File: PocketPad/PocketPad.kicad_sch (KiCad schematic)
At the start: 41 parts, among them SW0 SW_Push, SW1 SW_Push, SW10 SW_Push, SW11 SW_Push, SW12 SW_Push, SW13 SW_Push, SW14 SW_Push, SW15 SW_Push, SW16 SW_Push, SW17 SW_Push, SW18 SW_Push, SW2 SW_Push, SW3 SW_Push, SW4 SW_Push, SW5 SW_Push, SW6 SW_Push, SW7 SW_Push, SW8 SW_Push, SW9 SW_Push

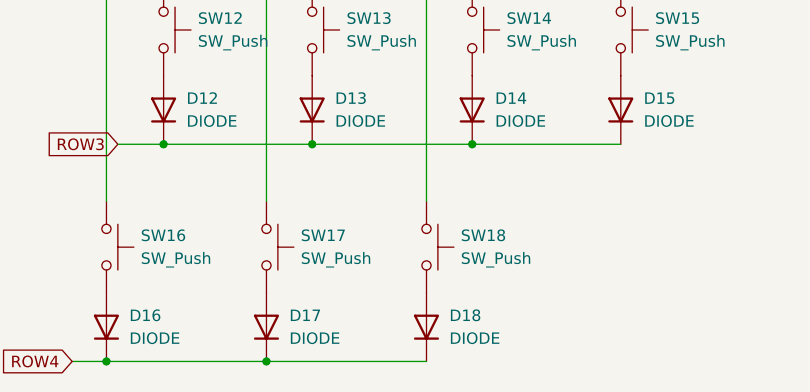
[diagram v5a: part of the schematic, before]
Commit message: V0.2 : Removed SW18
Redid trace routes. Removed SW18, moved SW16,17 over. Moved PWR & ACT LEDs
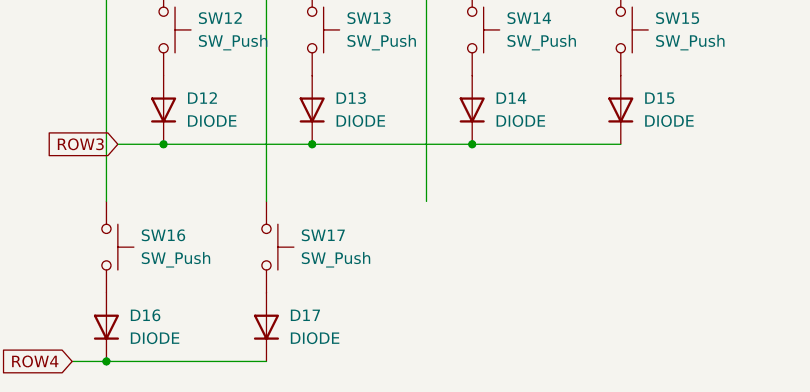
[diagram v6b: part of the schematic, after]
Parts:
- removed D18: DIODE, Diode_THT:D_DO-35_SOD27_P7.62mm_Horizontal, symbol Simulation_SPICE:DIODE
- removed SW18: SW_Push, Keebio:Switch_THT_6x6x8.5, symbol Switch:SW_Push
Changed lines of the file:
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@@
   (junction (at 102.87 67.31) (diameter 0) (color 0 0 0 0)
   )
-  (junction (at 91.44 129.54) (diameter 0) (color 0 0 0 0)
-  )
   (junction (at 100.33 43.18) (diameter 0) (color 0 0 0 0)
   )
@@
   )
   (wire (pts (xy 96.52 105.41) (xy 114.3 105.41))
-    (stroke (width 0) (type default) (color 0 0 0 0))
-  )
-  (wire (pts (xy 91.44 129.54) (xy 109.22 129.54))
     (stroke (width 0) (type default) (color 0 0 0 0))
   )
@@
     (pin "2")
   )
-  (symbol (lib_id "Switch:SW_Push") (at 109.22 116.84 270) (unit 1)
-    (in_bom yes) (on_board yes) (fields_autoplaced)
-    (property "Reference" "SW18" (id 0) (at 113.03 115.5699 90)
-      (effects (font (size 1.27 1.27)) (justify left))
-    )
-    (property "Value" "SW_Push" (id 1) (at 113.03 118.1099 90)
-      (effects (font (size 1.27 1.27)) (justify left))
-    )
-    (property "Footprint" "Keebio:Switch_THT_6x6x8.5" (id 2) (at 114.3 116.84 0)
-      (effects (font (size 1.27 1.27)) hide)
-    )
-    (property "Datasheet" "~" (id 3) (at 114.3 116.84 0)
-      (effects (font (size 1.27 1.27)) hide)
-    )
-    (pin "1")
-    (pin "2")
-  )
   (symbol (lib_id "Simulation_SPICE:DIODE") (at 116.84 39.37 270) (unit 1)
     (in_bom yes) (on_board yes) (fields_autoplaced)
@@
     (property "Datasheet" "~" (id 3) (at 133.35 50.8 0)
       (effects (font (size 1.27 1.27)) hide)
-    )
-    (pin "1")
-    (pin "2")
-  )
-  (symbol (lib_id "Simulation_SPICE:DIODE") (at 109.22 125.73 270) (unit 1)
-    (in_bom yes) (on_board yes) (fields_autoplaced)
-    (property "Reference" "D18" (id 0) (at 111.76 124.4599 90)
-      (effects (font (size 1.27 1.27)) (justify left))
-    )
-    (property "Value" "DIODE" (id 1) (at 111.76 126.9999 90)
-      (effects (font (size 1.27 1.27)) (justify left))
-    )
-    (property "Footprint" "Diode_THT:D_DO-35_SOD27_P7.62mm_Horizontal" (id 2) (at 109.22 125.73 0)
-      (effects (font (size 1.27 1.27)) hide)
-    )
-    (property "Datasheet" "~" (id 3) (at 109.22 125.73 0)
-      (effects (font (size 1.27 1.27)) hide)
-    )
-    (property "Spice_Netlist_Enabled" "Y" (id 4) (at 109.22 125.73 0)
-      (effects (font (size 1.27 1.27)) (justify left) hide)
-    )
-    (property "Spice_Primitive" "D" (id 5) (at 109.22 125.73 0)
-      (effects (font (size 1.27 1.27)) (justify left) hide)
     )
     (pin "1")
@@
       (reference "D17") (unit 1) (value "DIODE") (footprint "Diode_THT:D_DO-35_SOD27_P7.62mm_Horizontal")
     )
-    (path "/4d9a6203-d8f3-47c1-9521-23a9923c6132"
-      (reference "D18") (unit 1) (value "DIODE") (footprint "Diode_THT:D_DO-35_SOD27_P7.62mm_Horizontal")
-    )
     (path "/997ac6b3-feea-4945-b5ae-fc1302bd8731"
       (reference "MCU1") (unit 1) (value "Elite-C") (footprint "Keebio:Elite-C")
@@
       (reference "SW17") (unit 1) (value "SW_Push") (footprint "Keebio:Switch_THT_6x6x8.5")
     )
-    (path "/3ee2405a-2fc8-460e-9619-5b5c330637fc"
-      (reference "SW18") (unit 1) (value "SW_Push") (footprint "Keebio:Switch_THT_6x6x8.5")
-    )
-  )
+  )

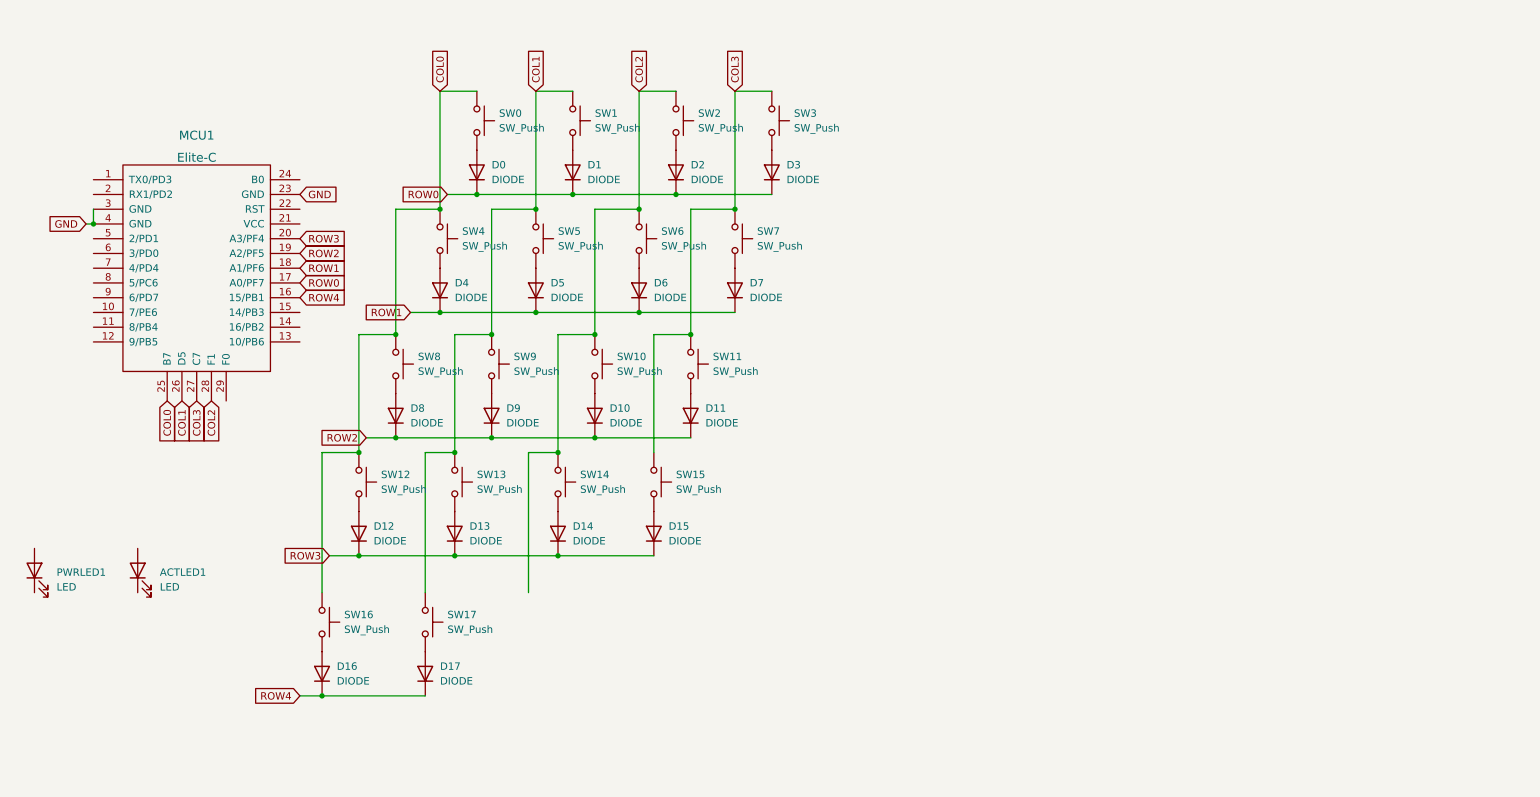
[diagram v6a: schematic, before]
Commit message: symbols updated. PCB redone.
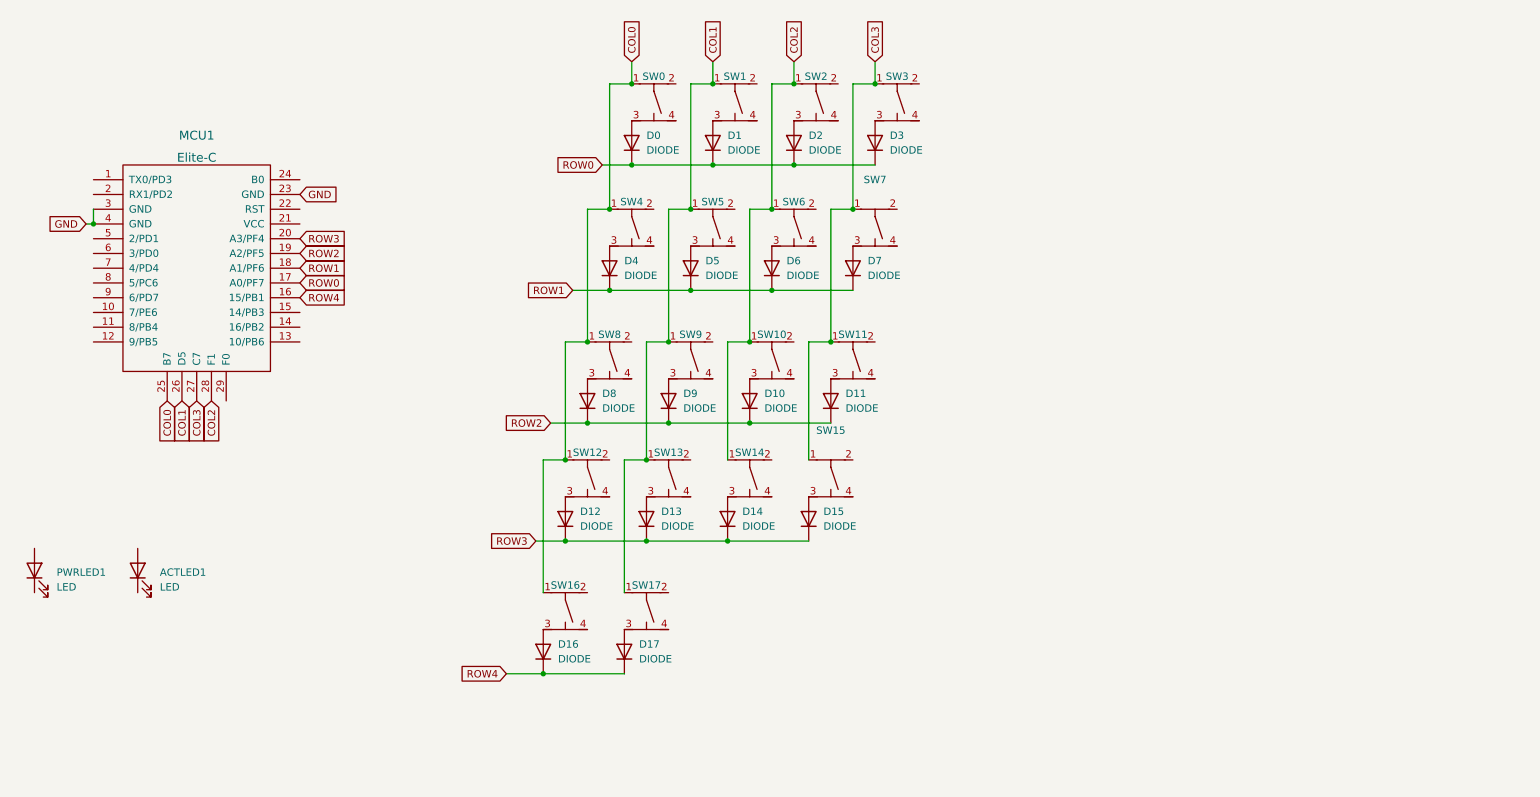
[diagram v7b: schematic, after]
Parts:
- removed SW0, SW1, SW10, SW11, SW12, SW13, SW14, SW15, SW16, SW17, SW2, SW3, SW4, SW5, SW6, SW7, SW8, SW9: SW_Push, Keebio:Switch_THT_6x6x8.5, symbol Switch:SW_Push
- added SW0, SW1, SW10, SW11, SW12, SW13, SW14, SW15, SW16, SW17, SW2, SW3, SW4, SW5, SW6, SW7, SW8, SW9: SW_THT_6x6, Keebio:Switch_THT_6x6x8.5, symbol MechBoards:SW_THT_6x6
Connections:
- net COL0: now also SW0.1, SW12.1, SW16.1, SW4.1, SW8.1
- net COL1: now also SW1.1, SW13.1, SW17.1, SW5.1, SW9.1
- net COL2: now also SW10.1, SW14.1, SW2.1, SW6.1
- net COL3: now also SW11.1, SW15.1, SW3.1, SW7.1
- net at D10.1 (A): now also SW10.3
- net at D8.1 (A): now also SW8.3
- net at D6.1 (A): now also SW6.3
- net at D13.1 (A): now also SW13.3
- net at D1.1 (A): now also SW1.3
- net at D4.1 (A): now also SW4.3
- net at D0.1 (A): now also SW0.3
- net at D14.1 (A): now also SW14.3
- net at D12.1 (A): now also SW12.3
- net at D15.1 (A): now also SW15.3
- net at D2.1 (A): now also SW2.3
- net at D5.1 (A): now also SW5.3
- net at D3.1 (A): now also SW3.3
- net at D11.1 (A): now also SW11.3
- net at D16.1 (A): now also SW16.3
- net at D7.1 (A): now also SW7.3
- net at D9.1 (A): now also SW9.3
- net at D17.1 (A): now also SW17.3
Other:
- moved on the sheet: D1, D10, D11, D13, D14, D15, D16, D17, D2, D3, D5, D6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

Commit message: V1 complete
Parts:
- added ACT-R1, PWR-R1: 1k, Resistor_THT:R_Axial_DIN0207_L6.3mm_D2.5mm_P10.16mm_Horizontal, symbol Device:R
- renumbered ACTLED1 to ACT1, PWRLED1 to PWR1
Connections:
- net COL0: now also MCU1.28 (F1); no longer MCU1.25 (B7)
- net COL1: now also MCU1.27 (C7); no longer MCU1.26 (D5)
- net COL2: now also MCU1.26 (D5); no longer MCU1.28 (F1)
- net COL3: now also MCU1.25 (B7); no longer MCU1.27 (C7)
- net GND: now also ACT-R1.2, PWR-R1.1
- net at ACT1.1 (K): now also ACT-R1.1
- net at ACT1.2 (A): now also MCU1.11 (8/PB4)
- net at MCU1.12 (9/PB5): now also PWR1.2 (A)
- net at PWR1.1 (K): now also PWR-R1.2
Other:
- moved on the sheet: ACT1, D0, D1, D10, D11, D12, D13, D14, D15, D16, D17, D2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
